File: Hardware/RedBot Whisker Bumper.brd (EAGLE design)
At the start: 25.4 x 17.8 mm, 9 parts

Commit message: Production Readied
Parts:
- added FID1, FID2: FIDUCIALUFIDUCIAL, SparkFun-Aesthetics:MICRO-FIDUCIAL
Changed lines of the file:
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@@
 <setting verticaltext="up"/>
 </settings>
-<grid distance="0.05" unitdist="inch" unit="inch" style="lines" multiple="1" display="yes" altdistance="0.005" altunitdist="inch" altunit="inch"/>
+<grid distance="0.05" unitdist="inch" unit="inch" style="lines" multiple="1" display="yes" altdistance="0.01" altunitdist="inch" altunit="inch"/>
 <layers>
 <layer number="1" name="Top" color="4" fill="1" visible="yes" active="yes"/>
@@
 <layer number="18" name="Vias" color="2" fill="1" visible="yes" active="yes"/>
 <layer number="19" name="Unrouted" color="6" fill="1" visible="yes" active="yes"/>
-<layer number="20" name="Dimension" color="15" fill="1" visible="yes" active="yes"/>
-<layer number="21" name="tPlace" color="16" fill="1" visible="yes" active="yes"/>
-<layer number="22" name="bPlace" color="14" fill="1" visible="yes" active="yes"/>
+<layer number="20" name="Dimension" color="6" fill="1" visible="yes" active="yes"/>
+<layer number="21" name="tPlace" color="6" fill="1" visible="yes" active="yes"/>
+<layer number="22" name="bPlace" color="6" fill="1" visible="yes" active="yes"/>
 <layer number="23" name="tOrigins" color="15" fill="1" visible="yes" active="yes"/>
 <layer number="24" name="bOrigins" color="15" fill="1" visible="yes" active="yes"/>
@@
 <element name="LOGO3" library="SparkFun-Aesthetics" package="OSHW-LOGO-S" value="OSHW-LOGOS" x="6.35" y="15.24" rot="MR0"/>
 <element name="LOGO4" library="SparkFun-Aesthetics" package="SFE-LOGO-FLAME" value="LOGO-SFESK" x="3.81" y="13.97" rot="MR0"/>
+<element name="FID1" library="SparkFun-Aesthetics" package="MICRO-FIDUCIAL" value="FIDUCIALUFIDUCIAL" x="0.762" y="0.762"/>
+<element name="FID2" library="SparkFun-Aesthetics" package="MICRO-FIDUCIAL" value="FIDUCIALUFIDUCIAL" x="24.13" y="16.51"/>
 </elements>
 <signals>

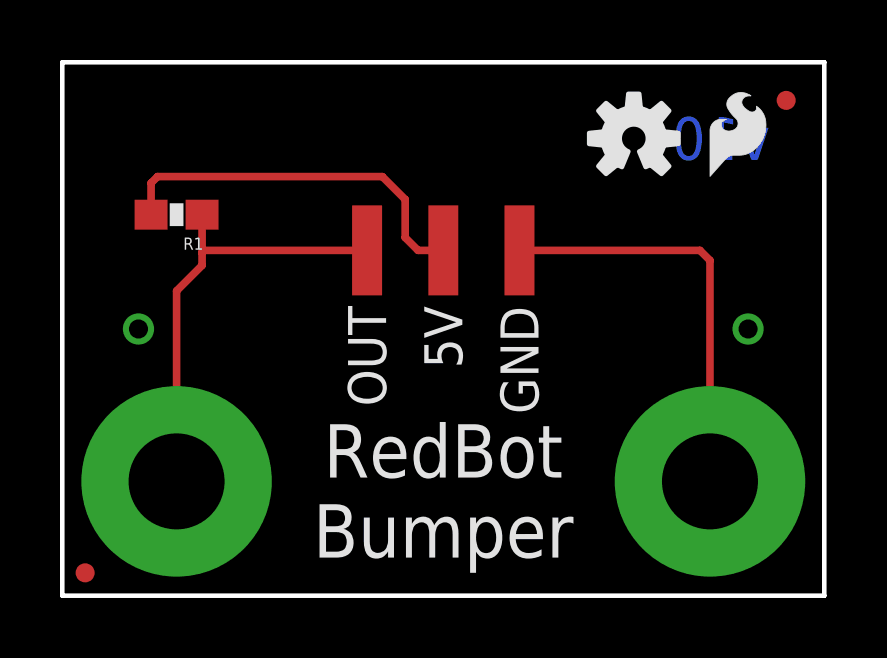
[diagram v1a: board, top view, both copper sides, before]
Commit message: QC Revision
Changes:
1.) New 3-pin SMD header footprints w/ bosses
2.) Moved R1 position and routing for better reflow
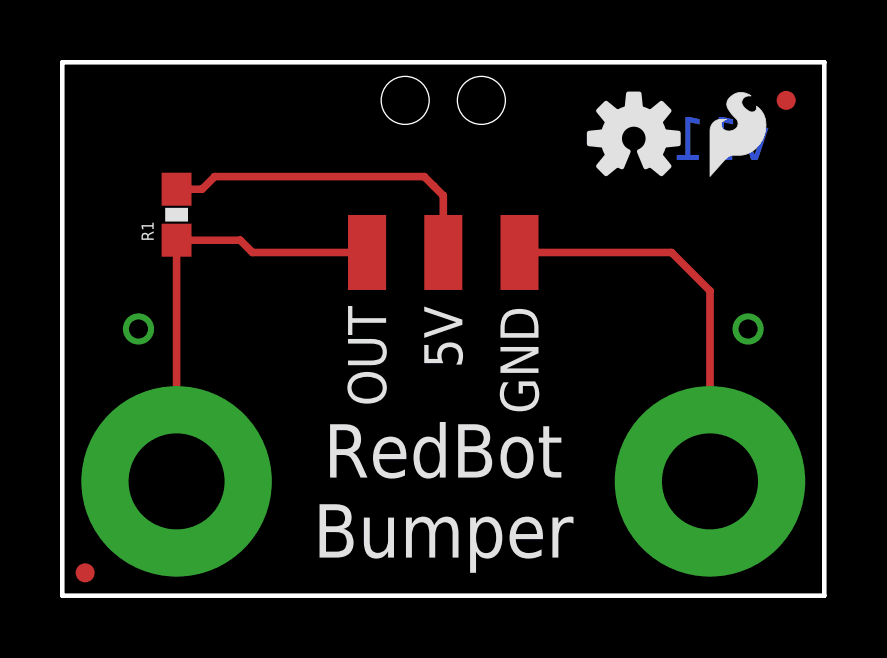
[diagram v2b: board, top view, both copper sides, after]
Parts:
- JP1: device SparkFun-Connectors:1X03_SMD_RA_MALE -> SparkFun-Connectors:1X03_SMD_RA_MALE_POST
- moved FRAME1 67.2 mm to (-15.2, -10.2)
- turned R1 to 90 degrees
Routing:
- net 5V: track 12.6 -> 11.2 mm
- net GND: track 13.9 -> 13.2 mm
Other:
- board text added: "Mike Hord"
- board text added: "Revision: Kade Jensen"
- board text added: "v11"
- board text removed: "v10"
